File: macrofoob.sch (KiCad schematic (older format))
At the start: 85 parts, among them J1 SSD1306 128x32 OLED, Q1 2N 2222A, SW1 Switch, SW10 Switch, SW11 Switch, SW12 Switch, SW13 Switch, SW14 Switch, SW15 Switch, SW16 Switch, SW17 Switch, SW18 Switch, SW19 Switch, SW2 Switch, SW20 Switch, SW21 Switch, SW22 Switch, SW23 Switch, SW24 Switch, SW25 Switch, SW3 Switch, SW4 Switch, SW5 Switch, SW6 Switch, SW7 Switch, SW8 Switch, SW9 Switch

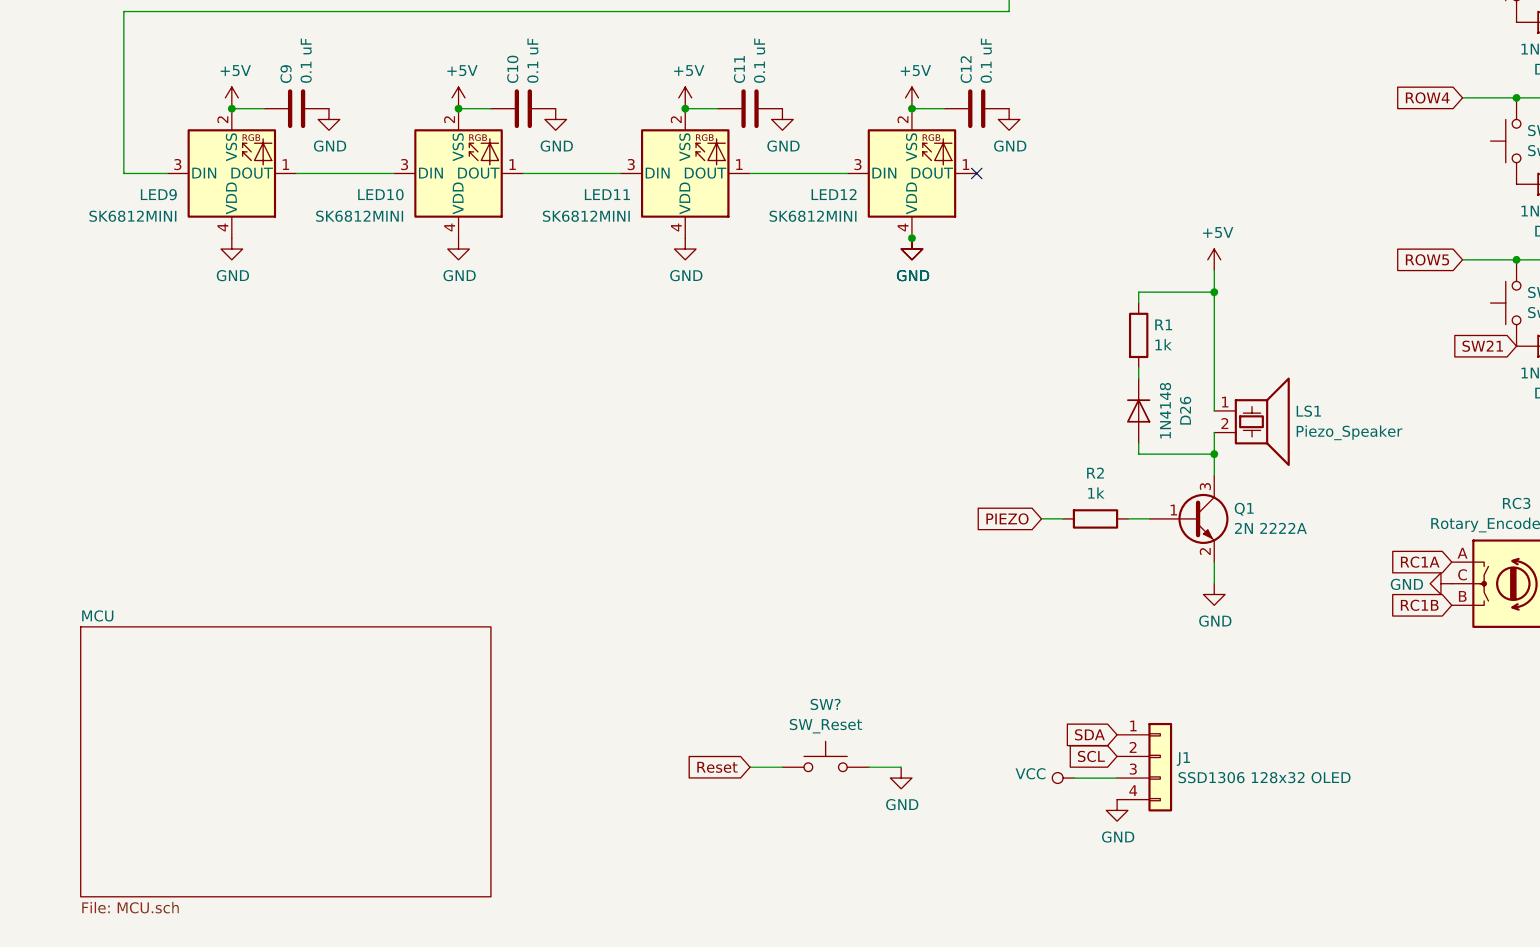
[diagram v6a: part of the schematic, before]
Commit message: added new TQFP-44 footprint with shorter pads
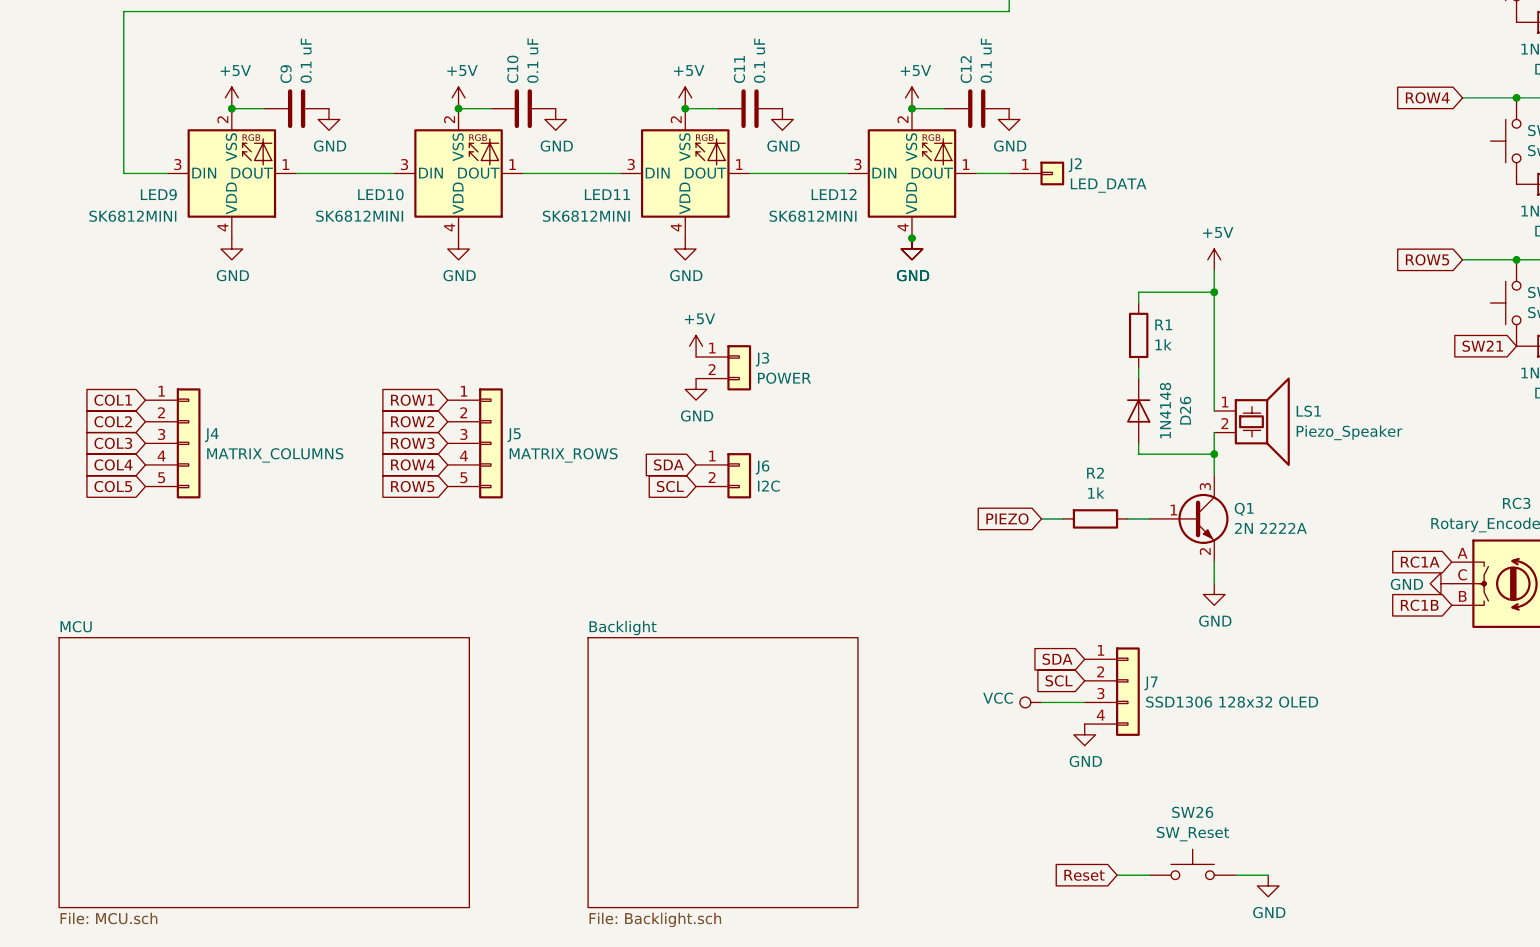
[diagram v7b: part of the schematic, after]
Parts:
- added J2: LED_DATA, symbol Connector_Generic:Conn_01x01
- added J3: POWER, symbol Connector_Generic:Conn_01x02
- added J4: MATRIX_COLUMNS, symbol Connector_Generic:Conn_01x05
- added J5: MATRIX_ROWS, symbol Connector_Generic:Conn_01x05
- added J6: I2C, symbol Connector_Generic:Conn_01x02
- gave numbers to parts that had none: 1
- renumbered J1 to J7
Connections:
- net +5V: now also J3.1 (Pin_1)
- net COL1: now also J4.1 (Pin_1)
- net COL2: now also J4.2 (Pin_2)
- net COL3: now also J4.3 (Pin_3)
- net COL4: now also J4.4 (Pin_4)
- net COL5: now also J4.5 (Pin_5)
- net GND: now also J3.2 (Pin_2)
- net ROW1: now also J5.1 (Pin_1)
- net ROW2: now also J5.2 (Pin_2)
- net ROW3: now also J5.3 (Pin_3)
- net ROW4: now also J5.4 (Pin_4)
- net ROW5: now also J5.5 (Pin_5)
- net SCL: now also J6.2 (Pin_2)
- net SDA: now also J6.1 (Pin_1)
- net at LED12.1 (DOUT): now also J2.1 (Pin_1)
- no-connect marks 1 -> 0
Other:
- moved on the sheet: J7, SW26
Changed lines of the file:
@@
 $Descr A4 11693 8268
 encoding utf-8
-Sheet 1 2
+Sheet 1 3
 Title ""
 Date ""
@@
 Wire Wire Line
 	1050 4100 1250 4100
-NoConn ~ 5000 4100
 $Comp
 L Device:Speaker_Crystal LS1
@@
 	1    0    0    -1
 $EndComp
-Text GLabel 5300 5700 0    50   Input ~ 0
-PIEZO
 $Comp
 L power:GND #PWR043
@@
 $EndComp
 $Comp
+L Device:Q_NPN_BEC Q1
+U 1 1 5D6AF1CE
+P 6000 5700
+F 0 "Q1" H 6191 5747 50  0000 L CNN
+F 1 "2N 2222A" H 6191 5654 50  0000 L CNN
+F 2 "Package_TO_SOT_SMD:SOT-23" H 6200 5800 50  0001 C CNN
+F 3 "~" H 6000 5700 50  0001 C CNN
+F 4 "https://www.reichelt.de/bipolartransistor-npn-40v-0-8a-0-4w-sot-23-2n-2222a-smd-p18407.html" H 6000 5700 50  0001 C CNN "URL"
+	1    6000 5700
+	1    0    0    -1
+$EndComp
+Wire Wire Line
+	5300 5700 5400 5700
+Wire Wire Line
+	5700 5700 5800 5700
+Wire Wire Line
+	6100 5900 6100 6000
+Wire Wire Line
+	6100 5500 6100 5400
+Wire Wire Line
+	5750 5350 5750 5400
+Wire Wire Line
+	5750 5400 6100 5400
+Connection ~ 6100 5400
+Wire Wire Line
+	6100 5400 6100 5300
+Wire Wire Line
+	6100 5200 6100 4650
+Wire Wire Line
+	6100 4650 5750 4650
+$Comp
+L power:+5V #PWR044
+U 1 1 5D6D3E04
+P 6100 4550
+F 0 "#PWR044" H 6100 4400 50  0001 C CNN
+F 1 "+5V" H 6115 4725 50  0000 C CNN
+F 2 "" H 6100 4550 50  0001 C CNN
+F 3 "" H 6100 4550 50  0001 C CNN
+	1    6100 4550
+	1    0    0    -1
+$EndComp
+Wire Wire Line
+	6100 4650 6100 4550
+Connection ~ 6100 4650
+Wire Wire Line
+	5750 4650 5750 4700
+Wire Wire Line
+	5750 5000 5750 5050
+$Comp
+L Connector_Generic:Conn_01x04 J7
+U 1 1 5D6C8E16
+P 5700 6450
+F 0 "J7" H 5780 6443 50  0000 L CNN
+F 1 "SSD1306 128x32 OLED" H 5780 6350 50  0000 L CNN
+F 2 "Connector_PinHeader_2.54mm:PinHeader_1x04_P2.54mm_Vertical" H 5700 6450 50  0001 C CNN
+F 3 "~" H 5700 6450 50  0001 C CNN
+	1    5700 6450
+	1    0    0    -1
+$EndComp
+$Comp
+L power:GND #PWR0101
+U 1 1 5D6CADAB
+P 5500 6650
+F 0 "#PWR0101" H 5500 6400 50  0001 C CNN
+F 1 "GND" H 5505 6475 50  0000 C CNN
+F 2 "" H 5500 6650 50  0001 C CNN
+F 3 "" H 5500 6650 50  0001 C CNN
+	1    5500 6650
+	1    0    0    -1
+$EndComp
+Text GLabel 5500 6450 0    50   Input ~ 0
+SCL
+Text GLabel 5500 6350 0    50   Input ~ 0
+SDA
+$Comp
+L power:VCC #PWR0103
+U 1 1 5D6CE66C
+P 5300 6550
+F 0 "#PWR0103" H 5300 6400 50  0001 C CNN
+F 1 "VCC" V 5318 6678 50  0000 L CNN
+F 2 "" H 5300 6550 50  0001 C CNN
+F 3 "" H 5300 6550 50  0001 C CNN
+	1    5300 6550
+	0    -1   -1   0
+$EndComp
+Wire Wire Line
+	5300 6550 5500 6550
+$Sheet
+S 750  6250 1900 1250
+U 5D7850B4
+F0 "MCU" 50
+F1 "MCU.sch" 50
+$EndSheet
+$Comp
+L Switch:SW_Push SW26
+U 1 1 5D815843
+P 6000 7350
+AR Path="/5D815843" Ref="SW26"  Part="1"
+AR Path="/5D7850B4/5D815843" Ref="SW?"  Part="1"
+F 0 "SW26" H 6000 7639 50  0000 C CNN
+F 1 "SW_Reset" H 6000 7546 50  0000 C CNN
+F 2 "Button_Switch_SMD:SW_SPST_PTS810" H 6000 7550 50  0001 C CNN
+F 3 "~" H 6000 7550 50  0001 C CNN
+F 4 "https://www.aliexpress.com/item/32837850387.html" H 6000 7350 50  0001 C CNN "URL"
+	1    6000 7350
+	1    0    0    -1
+$EndComp
+Text GLabel 5650 7350 0    50   Input ~ 0
+Reset
+$Comp
+L power:GND #PWR039
+U 1 1 5D81904B
+P 4700 4400
+F 0 "#PWR039" H 4700 4150 50  0001 C CNN
+F 1 "GND" H 4705 4225 50  0000 C CNN
+F 2 "" H 4700 4400 50  0001 C CNN
+F 3 "" H 4700 4400 50  0001 C CNN
+	1    4700 4400
+	1    0    0    -1
+$EndComp
+Connection ~ 4700 4400
+$Comp
+L power:GND #PWR046
+U 1 1 5D819078
+P 6350 7350
+F 0 "#PWR046" H 6350 7100 50  0001 C CNN
+F 1 "GND" H 6355 7175 50  0000 C CNN
+F 2 "" H 6350 7350 50  0001 C CNN
+F 3 "" H 6350 7350 50  0001 C CNN
+	1    6350 7350
+	1    0    0    -1
+$EndComp
+Wire Wire Line
+	5650 7350 5800 7350
+Wire Wire Line
+	6200 7350 6350 7350
+$Comp
+L Connector_Generic:Conn_01x02 J3
+U 1 1 5D74E4BE
+P 3900 4950
+F 0 "J3" H 3980 4943 50  0000 L CNN
+F 1 "POWER" H 3980 4850 50  0000 L CNN
+F 2 "" H 3900 4950 50  0001 C CNN
+F 3 "~" H 3900 4950 50  0001 C CNN
+	1    3900 4950
+	1    0    0    -1
+$EndComp
+$Comp
+L Connector_Generic:Conn_01x02 J6
+U 1 1 5D74F5A4
+P 3900 5450
+F 0 "J6" H 3980 5443 50  0000 L CNN
+F 1 "I2C" H 3980 5350 50  0000 L CNN
+F 2 "" H 3900 5450 50  0001 C CNN
+F 3 "~" H 3900 5450 50  0001 C CNN
+	1    3900 5450
+	1    0    0    -1
+$EndComp
+$Comp
+L Connector_Generic:Conn_01x05 J5
+U 1 1 5D7503CC
+P 2750 5350
+F 0 "J5" H 2830 5393 50  0000 L CNN
+F 1 "MATRIX_ROWS" H 2830 5300 50  0000 L CNN
+F 2 "" H 2750 5350 50  0001 C CNN
+F 3 "~" H 2750 5350 50  0001 C CNN
+	1    2750 5350
+	1    0    0    -1
+$EndComp
+$Comp
+L Connector_Generic:Conn_01x01 J2
+U 1 1 5D751619
+P 5350 4100
+F 0 "J2" H 5429 4143 50  0000 L CNN
+F 1 "LED_DATA" H 5429 4050 50  0000 L CNN
+F 2 "" H 5350 4100 50  0001 C CNN
+F 3 "~" H 5350 4100 50  0001 C CNN
+	1    5350 4100
+	1    0    0    -1
+$EndComp
+Wire Wire Line
+	5000 4100 5150 4100
+$Comp
+L Connector_Generic:Conn_01x05 J4
+U 1 1 5D75615C
+P 1350 5350
+F 0 "J4" H 1429 5393 50  0000 L CNN
+F 1 "MATRIX_COLUMNS" H 1429 5300 50  0000 L CNN
+F 2 "" H 1350 5350 50  0001 C CNN
+F 3 "~" H 1350 5350 50  0001 C CNN
+	1    1350 5350
+	1    0    0    -1
+$EndComp
+Text GLabel 3700 5450 0    50   Input ~ 0
+SDA
+Text GLabel 3700 5550 0    50   Input ~ 0
+SCL
+$Comp
+L power:GND #PWR045
+U 1 1 5D758616
+P 3700 5050
+F 0 "#PWR045" H 3700 4800 50  0001 C CNN
+F 1 "GND" H 3705 4875 50  0000 C CNN
+F 2 "" H 3700 5050 50  0001 C CNN
+F 3 "" H 3700 5050 50  0001 C CNN
+	1    3700 5050
+	1    0    0    -1
+$EndComp
+$Comp
+L power:+5V #PWR040
+U 1 1 5D758B00
+P 3700 4950
+F 0 "#PWR040" H 3700 4800 50  0001 C CNN
+F 1 "+5V" H 3715 5125 50  0000 C CNN
+F 2 "" H 3700 4950 50  0001 C CNN
+F 3 "" H 3700 4950 50  0001 C CNN
+	1    3700 4950
+	1    0    0    -1
+$EndComp
+Text GLabel 2550 5150 0    50   Input ~ 0
+ROW1
+Text GLabel 2550 5250 0    50   Input ~ 0
+ROW2
+Text GLabel 2550 5350 0    50   Input ~ 0
+ROW3
+Text GLabel 2550 5450 0    50   Input ~ 0
+ROW4
+Text GLabel 2550 5550 0    50   Input ~ 0
+ROW5
+Text GLabel 1150 5150 0    50   Input ~ 0
+COL1
+Text GLabel 1150 5250 0    50   Input ~ 0
+COL2
+Text GLabel 1150 5350 0    50   Input ~ 0
+COL3
+Text GLabel 1150 5450 0    50   Input ~ 0
+COL4
+Text GLabel 1150 5550 0    50   Input ~ 0
+COL5
+$Sheet
+S 3200 6250 1250 1250
+U 5D79FC99
+F0 "Backlight" 50
+F1 "Backlight.sch" 50
+$EndSheet
+Text GLabel 5300 5700 0    50   Input ~ 0
+PIEZO
+$Comp
 L Device:R R2
 U 1 1 5D6ACF2D
@@
 	0    1    1    0
 $EndComp
-$Comp
-L Device:Q_NPN_BEC Q1
-U 1 1 5D6AF1CE
-P 6000 5700
-F 0 "Q1" H 6191 5747 50  0000 L CNN
-F 1 "2N 2222A" H 6191 5654 50  0000 L CNN
-F 2 "Package_TO_SOT_SMD:SOT-23" H 6200 5800 50  0001 C CNN
-F 3 "~" H 6000 5700 50  0001 C CNN
-F 4 "https://www.reichelt.de/bipolartransistor-npn-40v-0-8a-0-4w-sot-23-2n-2222a-smd-p18407.html" H 6000 5700 50  0001 C CNN "URL"
-	1    6000 5700
-	1    0    0    -1
-$EndComp
-Wire Wire Line
-	5300 5700 5400 5700
-Wire Wire Line
-	5700 5700 5800 5700
-Wire Wire Line
-	6100 5900 6100 6000
-Wire Wire Line
-	6100 5500 6100 5400
-Wire Wire Line
-	5750 5350 5750 5400
-Wire Wire Line
-	5750 5400 6100 5400
-Connection ~ 6100 5400
-Wire Wire Line
-	6100 5400 6100 5300
-Wire Wire Line
-	6100 5200 6100 4650
-Wire Wire Line
-	6100 4650 5750 4650
-$Comp
-L power:+5V #PWR044
-U 1 1 5D6D3E04
-P 6100 4550
-F 0 "#PWR044" H 6100 4400 50  0001 C CNN
-F 1 "+5V" H 6115 4725 50  0000 C CNN
-F 2 "" H 6100 4550 50  0001 C CNN
-F 3 "" H 6100 4550 50  0001 C CNN
-	1    6100 4550
-	1    0    0    -1
-$EndComp
-Wire Wire Line
-	6100 4650 6100 4550
-Connection ~ 6100 4650
-Wire Wire Line
-	5750 4650 5750 4700
-Wire Wire Line
-	5750 5000 5750 5050
-$Comp
-L Connector_Generic:Conn_01x04 J1
-U 1 1 5D6C8E16
-P 5850 6800
-F 0 "J1" H 5930 6793 50  0000 L CNN
-F 1 "SSD1306 128x32 OLED" H 5930 6700 50  0000 L CNN
-F 2 "Connector_PinHeader_2.54mm:PinHeader_1x04_P2.54mm_Vertical" H 5850 6800 50  0001 C CNN
-F 3 "~" H 5850 6800 50  0001 C CNN
-	1    5850 6800
-	1    0    0    -1
-$EndComp
-$Comp
-L power:GND #PWR0101
-U 1 1 5D6CADAB
-P 5650 7000
-F 0 "#PWR0101" H 5650 6750 50  0001 C CNN
-F 1 "GND" H 5655 6825 50  0000 C CNN
-F 2 "" H 5650 7000 50  0001 C CNN
-F 3 "" H 5650 7000 50  0001 C CNN
-	1    5650 7000
-	1    0    0    -1
-$EndComp
-Text GLabel 5650 6800 0    50   Input ~ 0
-SCL
-Text GLabel 5650 6700 0    50   Input ~ 0
-SDA
-$Comp
-L power:VCC #PWR0103
-U 1 1 5D6CE66C
-P 5450 6900
-F 0 "#PWR0103" H 5450 6750 50  0001 C CNN
-F 1 "VCC" V 5468 7028 50  0000 L CNN
-F 2 "" H 5450 6900 50  0001 C CNN
-F 3 "" H 5450 6900 50  0001 C CNN
-	1    5450 6900
-	0    -1   -1   0
-$EndComp
-Wire Wire Line
-	5450 6900 5650 6900
-$Sheet
-S 850  6200 1900 1250
-U 5D7850B4
-F0 "MCU" 50
-F1 "MCU.sch" 50
-$EndSheet
-$Comp
-L Switch:SW_Push SW?
-U 1 1 5D815843
-P 4300 6850
-AR Path="/5D815843" Ref="SW?"  Part="1"
-AR Path="/5D7850B4/5D815843" Ref="SW?"  Part="1"
-F 0 "SW?" H 4300 7139 50  0000 C CNN
-F 1 "SW_Reset" H 4300 7046 50  0000 C CNN
-F 2 "Button_Switch_SMD:SW_SPST_PTS810" H 4300 7050 50  0001 C CNN
-F 3 "~" H 4300 7050 50  0001 C CNN
-F 4 "https://www.aliexpress.com/item/32837850387.html" H 4300 6850 50  0001 C CNN "URL"
-	1    4300 6850
-	1    0    0    -1
-$EndComp
-Text GLabel 3950 6850 0    50   Input ~ 0
-Reset
-$Comp
-L power:GND #PWR?
-U 1 1 5D81904B
-P 4700 4400
-F 0 "#PWR?" H 4700 4150 50  0001 C CNN
-F 1 "GND" H 4705 4225 50  0000 C CNN
-F 2 "" H 4700 4400 50  0001 C CNN
-F 3 "" H 4700 4400 50  0001 C CNN
-	1    4700 4400
-	1    0    0    -1
-$EndComp
-Connection ~ 4700 4400
-$Comp
-L power:GND #PWR?
-U 1 1 5D819078
-P 4650 6850
-F 0 "#PWR?" H 4650 6600 50  0001 C CNN
-F 1 "GND" H 4655 6675 50  0000 C CNN
-F 2 "" H 4650 6850 50  0001 C CNN
-F 3 "" H 4650 6850 50  0001 C CNN
-	1    4650 6850
-	1    0    0    -1
-$EndComp
-Wire Wire Line
-	3950 6850 4100 6850
-Wire Wire Line
-	4500 6850 4650 6850
 $EndSCHEMATC

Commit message: added new generic SMD pad footprints and footprint associations
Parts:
- J2: footprint (none) -> testatur:Generic_Pads_2mm_1x1
- J3, J6: footprint (none) -> testatur:Generic_Pads_2mm_1x2
- J4, J5: footprint (none) -> testatur:Generic_Pads_2mm_1x5
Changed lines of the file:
@@
 F 0 "J3" H 3980 4943 50  0000 L CNN
 F 1 "POWER" H 3980 4850 50  0000 L CNN
-F 2 "" H 3900 4950 50  0001 C CNN
+F 2 "testatur:Generic_Pads_2mm_1x2" H 3900 4950 50  0001 C CNN
 F 3 "~" H 3900 4950 50  0001 C CNN
 	1    3900 4950
@@
 F 0 "J6" H 3980 5443 50  0000 L CNN
 F 1 "I2C" H 3980 5350 50  0000 L CNN
-F 2 "" H 3900 5450 50  0001 C CNN
+F 2 "testatur:Generic_Pads_2mm_1x2" H 3900 5450 50  0001 C CNN
 F 3 "~" H 3900 5450 50  0001 C CNN
 	1    3900 5450
@@
 F 0 "J5" H 2830 5393 50  0000 L CNN
 F 1 "MATRIX_ROWS" H 2830 5300 50  0000 L CNN
-F 2 "" H 2750 5350 50  0001 C CNN
+F 2 "testatur:Generic_Pads_2mm_1x5" H 2750 5350 50  0001 C CNN
 F 3 "~" H 2750 5350 50  0001 C CNN
 	1    2750 5350
@@
 F 0 "J2" H 5429 4143 50  0000 L CNN
 F 1 "LED_DATA" H 5429 4050 50  0000 L CNN
-F 2 "" H 5350 4100 50  0001 C CNN
+F 2 "testatur:Generic_Pads_2mm_1x1" H 5350 4100 50  0001 C CNN
 F 3 "~" H 5350 4100 50  0001 C CNN
 	1    5350 4100
@@
 F 0 "J4" H 1429 5393 50  0000 L CNN
 F 1 "MATRIX_COLUMNS" H 1429 5300 50  0000 L CNN
-F 2 "" H 1350 5350 50  0001 C CNN
+F 2 "testatur:Generic_Pads_2mm_1x5" H 1350 5350 50  0001 C CNN
 F 3 "~" H 1350 5350 50  0001 C CNN
 	1    1350 5350
